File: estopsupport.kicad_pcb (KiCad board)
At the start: 2 copper layers, 65 x 35 mm, 23 parts, among them J1 ESTOP1, J2 ESTOP2, J3 CONTACTOR, J4 TAP_ESTOP, J5 5V_IN, J6 PWR, U1 PC817, U2 BTS6163D

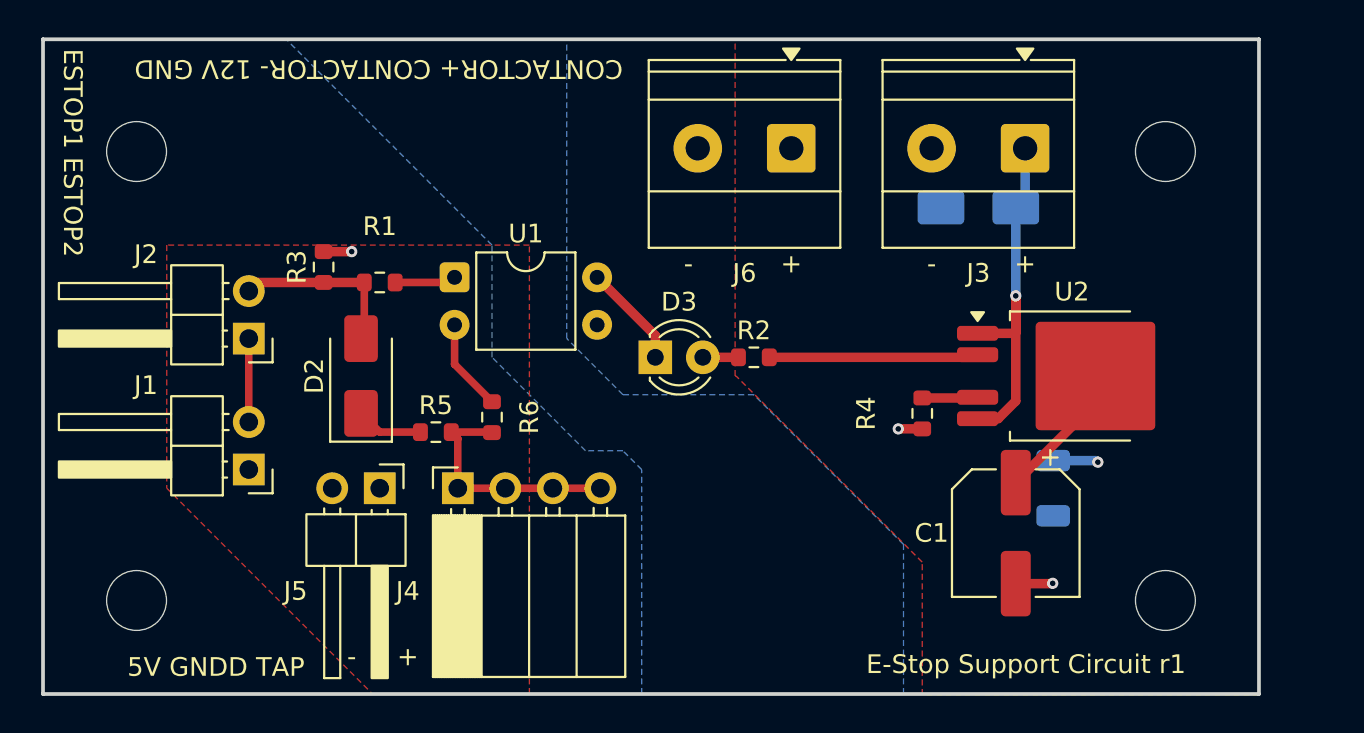
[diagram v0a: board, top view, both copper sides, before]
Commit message: refactor: use a tht resistor for the shunt - easier to probe and replace
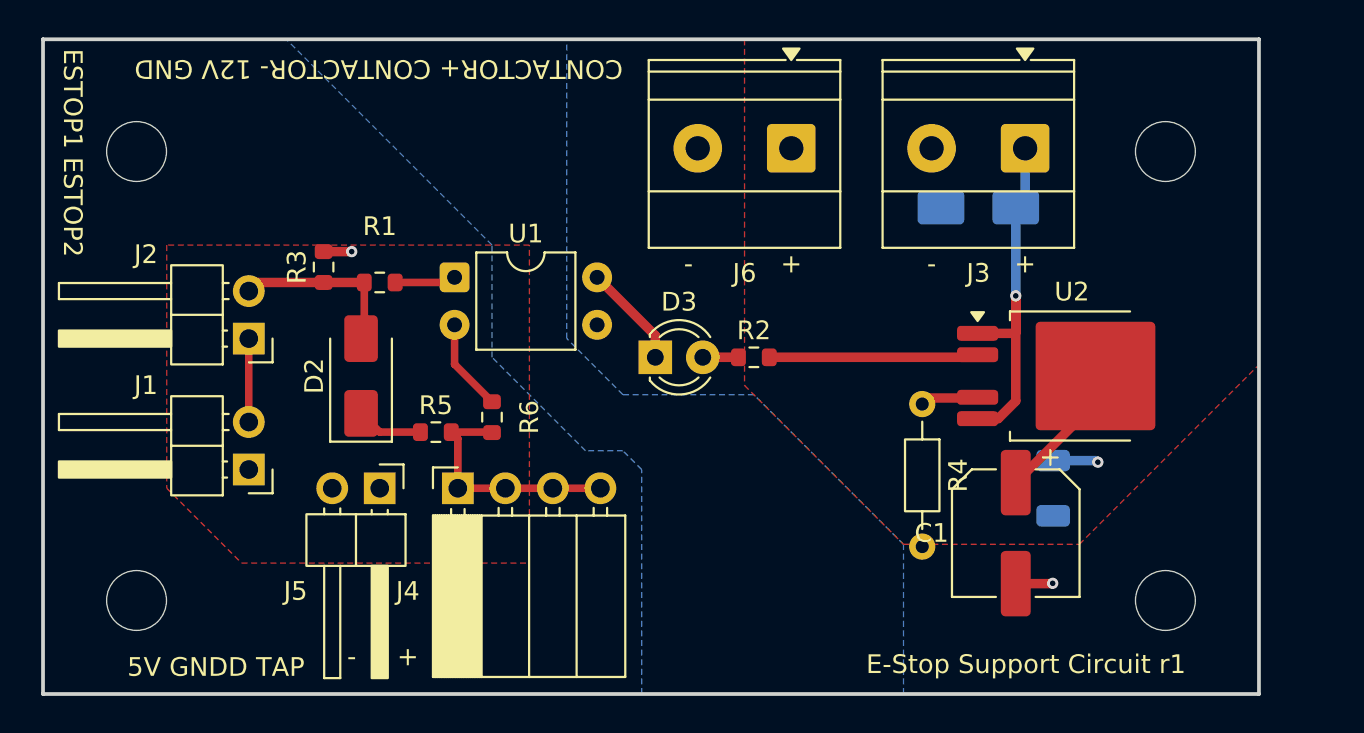
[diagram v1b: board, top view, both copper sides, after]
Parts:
- R4: footprint Resistor_SMD:R_0603_1608Metric -> Resistor_THT:R_Axial_DIN0204_L3.6mm_D1.6mm_P7.62mm_Horizontal
- moved R4 0.50 mm to (82.0, 50.8)
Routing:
- net GND: track 3.26 -> 1.98 mm, vias 2 -> 1
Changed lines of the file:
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@@
 		(capping no)
 		(filling no)
-		(zone_defaults)
 		(grid_origin 35 31.275)
 		(pcbplotparams
@@
 		(embedded_fonts no)
 	)
-	(footprint "Resistor_SMD:R_0603_1608Metric"
+	(footprint "Resistor_THT:R_Axial_DIN0204_L3.6mm_D1.6mm_P7.62mm_Horizontal"
 		(layer "F.Cu")
-		(at 82 51.275 -90)
-		(descr "Resistor SMD 0603 (1608 Metric), square (rectangular) end terminal, IPC-7351 nominal, (Body size source: IPC-SM-782 page 72, https://www.pcb-3d.com/wordpress/wp-content/uploads/ipc-sm-782a_amendment_1_and_2.pdf)")
-		(tags "resistor")
+		(at 82 50.775 -90)
+		(descr "Resistor, Axial_DIN0204 series, Axial, Horizontal, pin pitch=7.62mm, 0.167W, length*diameter=3.6*1.6mm^2, http://cdn-reichelt.de/documents/datenblatt/B400/1_4W%23YAG.pdf")
+		(tags "Resistor Axial_DIN0204 series Axial Horizontal pin pitch 7.62mm 0.167W length 3.6mm diameter 1.6mm")
 		(property "Reference" "R4"
-			(at 0 3 270)
+			(at 3.81 -1.92 270)
 			(layer "F.SilkS")
 			(effects
@@
 		)
 		(property "Value" "10k"
-			(at 0 1.43 270)
+			(at 3.81 1.92 270)
 			(layer "F.Fab")
 			(effects
@@
 			)
 		)
-		(attr smd)
+		(attr through_hole)
 		(duplicate_pad_numbers_are_jumpers no)
 		(fp_line
-			(start -0.237258 0.5225)
-			(end 0.237258 0.5225)
+			(start 0.94 0)
+			(end 1.89 0)
 			(stroke
 				(width 0.12)
@@
 		)
 		(fp_line
-			(start -0.237258 -0.5225)
-			(end 0.237258 -0.5225)
+			(start 6.68 0)
+			(end 5.73 0)
 			(stroke
 				(width 0.12)
@@
 		)
 		(fp_rect
-			(start -1.48 -0.73)
-			(end 1.48 0.73)
+			(start 1.89 -0.92)
+			(end 5.73 0.92)
+			(stroke
+				(width 0.12)
+				(type solid)
+			)
+			(fill no)
+			(layer "F.SilkS")
+		)
+		(fp_rect
+			(start -0.95 -1.05)
+			(end 8.57 1.05)
 			(stroke
 				(width 0.05)
@@
 			(layer "F.CrtYd")
 		)
+		(fp_line
+			(start 0 0)
+			(end 2.01 0)
+			(stroke
+				(width 0.1)
+				(type solid)
+			)
+			(layer "F.Fab")
+		)
+		(fp_line
+			(start 7.62 0)
+			(end 5.61 0)
+			(stroke
+				(width 0.1)
+				(type solid)
+			)
+			(layer "F.Fab")
+		)
 		(fp_rect
-			(start -0.8 -0.4125)
-			(end 0.8 0.4125)
+			(start 2.01 -0.8)
+			(end 5.61 0.8)
 			(stroke
 				(width 0.1)
@@
 		)
 		(fp_text user "${REFERENCE}"
-			(at 0 0 270)
+			(at 3.81 0 270)
 			(layer "F.Fab")
 			(effects
 				(font
-					(size 0.4 0.4)
-					(thickness 0.06)
+					(size 0.72 0.72)
+					(thickness 0.108)
 				)
 			)
 		)
-		(pad "1" smd roundrect
-			(at -0.825 0 270)
-			(size 0.8 0.95)
-			(layers "F.Cu" "F.Mask" "F.Paste")
-			(roundrect_rratio 0.25)
+		(pad "1" thru_hole circle
+			(at 0 0 270)
+			(size 1.4 1.4)
+			(drill 0.7)
+			(layers "*.Cu" "*.Mask")
+			(remove_unused_layers no)
 			(net "Net-(U2-IS)")
 			(pintype "passive")
 		)
-		(pad "2" smd roundrect
-			(at 0.825 0 270)
-			(size 0.8 0.95)
-			(layers "F.Cu" "F.Mask" "F.Paste")
-			(roundrect_rratio 0.25)
+		(pad "2" thru_hole circle
+			(at 7.62 0 270)
+			(size 1.4 1.4)
+			(drill 0.7)
+			(layers "*.Cu" "*.Mask")
+			(remove_unused_layers no)
 			(net "GND")
 			(pintype "passive")
 		)
 		(embedded_fonts no)
-		(model "${KICAD10_3DMODEL_DIR}/Resistor_SMD.3dshapes/R_0603_1608Metric.step"
+		(model "${KICAD10_3DMODEL_DIR}/Resistor_THT.3dshapes/R_Axial_DIN0204_L3.6mm_D1.6mm_P7.62mm_Horizontal.step"
 			(offset
 				(xyz 0 0 0)
@@
 	)
 	(segment
-		(start 81.997 52.103)
-		(end 82 52.1)
-		(width 0.508)
-		(layer "F.Cu")
-		(net "GND")
-	)
-	(segment
 		(start 88.958003 60.374997)
 		(end 88.975 60.358)
@@
 		(net "GND")
 	)
-	(segment
-		(start 80.72 52.103)
-		(end 81.997 52.103)
-		(width 0.508)
-		(layer "F.Cu")
-		(net "GND")
-	)
-	(via
-		(at 80.72 52.103)
-		(size 0.6)
-		(drill 0.3)
-		(layers "F.Cu" "B.Cu")
-		(net "GND")
-	)
 	(via
 		(at 88.975 60.358)
@@
 	)
 	(segment
+		(start 84.925002 50.45)
+		(end 84.960002 50.415)
+		(width 0.508)
+		(layer "F.Cu")
+		(net "Net-(U2-IS)")
+	)
+	(segment
+		(start 82 50.45)
+		(end 84.925002 50.45)
+		(width 0.508)
+		(layer "F.Cu")
+		(net "Net-(U2-IS)")
+	)
+	(segment
+		(start 84.960001 48.236351)
+		(end 84.960001 48.135)
+		(width 0.508)
+		(layer "F.Cu")
+		(net "Net-(U2-IN)")
+	)
+	(segment
+		(start 84.921352 48.275)
+		(end 84.960001 48.236351)
+		(width 0.508)
+		(layer "F.Cu")
+		(net "Net-(U2-IN)")
+	)
+	(segment
+		(start 73.825 48.275)
+		(end 84.921352 48.275)
+		(width 0.508)
+		(layer "F.Cu")
+		(net "Net-(U2-IN)")
+	)
+	(segment
+		(start 53.825 44.275)
+		(end 56.725 44.275)
+		(width 0.4064)
+		(layer "F.Cu")
+		(net "Net-(R1-Pad2)")
+	)
+	(segment
+		(start 56.725 44.275)
+		(end 57 44)
+		(width 0.4064)
+		(layer "F.Cu")
+		(net "Net-(R1-Pad2)")
+	)
+	(segment
 		(start 87 46.967)
 		(end 86.972 46.995)
@@
 		(net "Net-(D1-K)")
 	)
-	(segment
-		(start 84.925002 50.45)
-		(end 84.960002 50.415)
-		(width 0.508)
-		(layer "F.Cu")
-		(net "Net-(U2-IS)")
-	)
-	(segment
-		(start 82 50.45)
-		(end 84.925002 50.45)
-		(width 0.508)
-		(layer "F.Cu")
-		(net "Net-(U2-IS)")
-	)
-	(segment
-		(start 84.960001 48.236351)
-		(end 84.960001 48.135)
-		(width 0.508)
-		(layer "F.Cu")
-		(net "Net-(U2-IN)")
-	)
-	(segment
-		(start 84.921352 48.275)
-		(end 84.960001 48.236351)
-		(width 0.508)
-		(layer "F.Cu")
-		(net "Net-(U2-IN)")
-	)
-	(segment
-		(start 73.825 48.275)
-		(end 84.921352 48.275)
-		(width 0.508)
-		(layer "F.Cu")
-		(net "Net-(U2-IN)")
-	)
-	(segment
-		(start 53.825 44.275)
-		(end 56.725 44.275)
-		(width 0.4064)
-		(layer "F.Cu")
-		(net "Net-(R1-Pad2)")
-	)
-	(segment
-		(start 56.725 44.275)
-		(end 57 44)
-		(width 0.4064)
-		(layer "F.Cu")
-		(net "Net-(R1-Pad2)")
-	)
 	(zone
-		(net "+5V")
+		(net "+12V")
 		(layer "F.Cu")
 		(hatch edge 0.5)
+		(priority 3)
 		(connect_pads
 			(clearance 0.5)
@@
 		(polygon
 			(pts
-				(xy 61 66.275) (xy 61 42.275) (xy 41.615 42.275) (xy 41.615 55.275) (xy 52.615 66.275)
+				(xy 100 31.275) (xy 72.5 31.275) (xy 72.5 49.775) (xy 81 58.275) (xy 90.399998 58.275) (xy 99.899998 48.775)
+				(xy 100 48.775)
 			)
 		)
 	)
 	(zone
-		(net "+12V")
+		(net "+5V")
 		(layer "F.Cu")
 		(hatch edge 0.5)
-		(priority 3)
 		(connect_pads
 			(clearance 0.5)
@@
 			(thermal_gap 0.5)
 			(thermal_bridge_width 0.5)
-			(smoothing fillet)
-			(radius 2)
 			(island_removal_mode 0)
 		)
 		(polygon
 			(pts
-				(xy 100 66.327) (xy 82 66.327) (xy 82 59.225) (xy 72.05 49.275) (xy 72 49.275) (xy 72 31.275) (xy 100 31.275)
+				(xy 61 59.275) (xy 61 42.275) (xy 41.615 42.275) (xy 41.615 55.275) (xy 45.615 59.275)
 			)
 		)
